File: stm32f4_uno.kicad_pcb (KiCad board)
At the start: 2 copper layers, 68.6 x 53.3 mm, 66 parts, among them J1 Barrel_Jack, J101 Digital/PWM, J102 Power, J103 Analog, J104 Digital/PWM, J105 Conn_ST_STDC14, J106 Ethernet, J107 STM32 GPIO, J108 STM32 GPIO, J109 STM32 GPIO, J110 STM32 GPIO, J111 STM32 GPIO, J2 SHOU HAN TYPE-C 16PIN 2MD(073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, U101 STM32F407VGT6, U201 AMS1117-5.0, U301 AMS1117-3.3, U501 SST26VF016BEUI-104I/SN, Y101 25MHz, Y102 32.768kHz

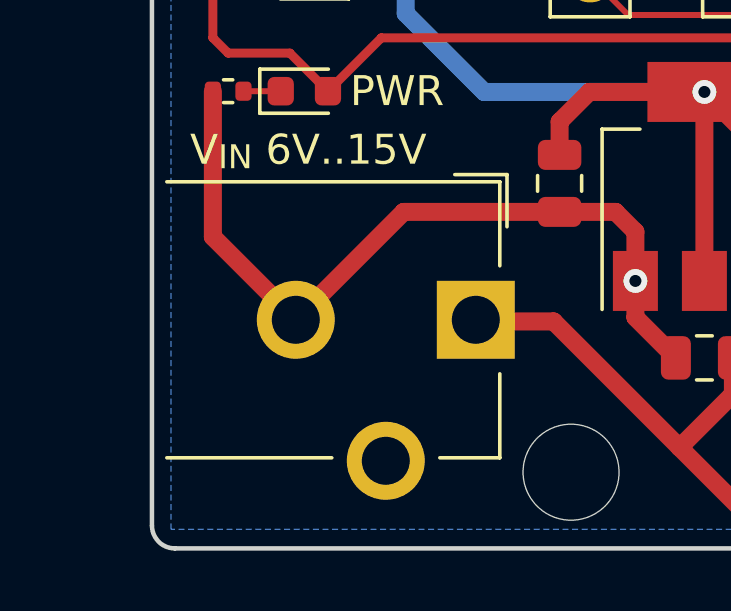
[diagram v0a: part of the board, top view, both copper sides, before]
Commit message: Add CUI Devices PJ-102AH 3D model and export PCB 3D model
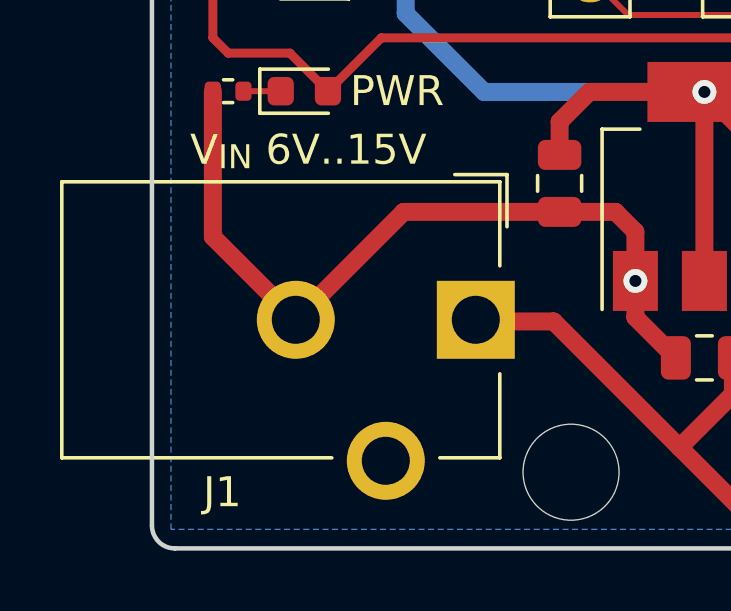
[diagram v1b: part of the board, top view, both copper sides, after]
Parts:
- J1: footprint Connector_BarrelJack:BarrelJack_CUI_PJ-102AH_Horizontal -> #Connector:CUI Devices PJ-102AH.pdf
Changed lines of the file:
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@@
     )
   )
-  (footprint "Connector_BarrelJack:BarrelJack_CUI_PJ-102AH_Horizontal" (layer "F.Cu")
+  (footprint "#Connector:CUI Devices PJ-102AH.pdf" (layer "F.Cu")
     (at 110.795 92.38 -90)
     (descr "Thin-pin DC Barrel Jack, https://cdn-shop.adafruit.com/datasheets/21mmdcjackDatasheet.pdf")
@@
     (property "Sheetfile" "stm32f4_uno.kicad_sch")
     (property "Sheetname" "")
-    (property "dnp" "")
     (property "exclude_from_bom" "")
     (property "isBasicPart" "NO")
@@
     (property "ki_keywords" "DC power barrel jack connector")
     (attr through_hole exclude_from_bom)
-    (fp_text reference "J1" (at 5.75 8.45) (layer "F.SilkS") hide
-        (effects (font (size 0.8 0.8) (thickness 0.15)))
-    )
-    (fp_text value "Barrel_Jack" (at -5.5 6.2) (layer "F.Fab") hide
-        (effects (font (size 0.8 0.8) (thickness 0.15)))
-    )
-    (fp_text user "${REFERENCE}" (at 0 6.5 90) (layer "F.Fab")
+    (fp_text reference "J1" (at 5.75 8.45) (layer "F.SilkS")
         (effects (font (size 1 1) (thickness 0.15)))
     )
+    (fp_text value "Barrel_Jack" (at -5.5 6.2) (layer "F.Fab")
+        (effects (font (size 1 1) (thickness 0.15)))
+    )
+    (fp_text user "${REFERENCE}" (at 0 6.5 -90) (layer "F.Fab")
+        (effects (font (size 1 1) (thickness 0.15)))
+    )
     (fp_line (start -4.84 -1.04) (end -3.1 -1.04)
       (stroke (width 0.12) (type solid)) (layer "F.SilkS"))
@@
     (fp_line (start -4.6 -0.8) (end -1.8 -0.8)
       (stroke (width 0.12) (type solid)) (layer "F.SilkS"))
-    (fp_line (start -4.6 10.3) (end -4.6 -0.8)
+    (fp_line (start -4.6 13.8) (end -4.6 -0.8)
       (stroke (width 0.12) (type solid)) (layer "F.SilkS"))
     (fp_line (start 1.8 -0.8) (end 4.6 -0.8)
@@
     (fp_line (start 4.6 -0.8) (end 4.6 1.2)
       (stroke (width 0.12) (type solid)) (layer "F.SilkS"))
-    (fp_line (start 4.6 4.8) (end 4.6 10.3)
+    (fp_line (start 4.6 4.8) (end 4.6 13.8)
+      (stroke (width 0.12) (type solid)) (layer "F.SilkS"))
+    (fp_line (start 4.6 13.8) (end -4.6 13.8)
       (stroke (width 0.12) (type solid)) (layer "F.SilkS"))
     (fp_line (start -5 -1.2) (end -1.8 -1.2)
@@
     (pad "3" thru_hole circle (at 4.7 3 270) (size 2.6 2.6) (drill 1.6) (layers "*.Cu" "*.Mask")
       (net 108 "unconnected-(J1-Pad3)") (pintype "passive+no_connect"))
-    (model "${KICAD6_3DMODEL_DIR}/Connector_BarrelJack.3dshapes/BarrelJack_CUI_PJ-102AH_Horizontal.wrl"
-      (offset (xyz 0 0 0))
-      (scale (xyz 1 1 1))
-      (rotate (xyz 0 0 0))
+    (model "${KIPRJMOD}/KiCad-Lib/#Connector.3dshapes/CUI Devices PJ-102AH.step"
+      (offset (xyz 0 -6.5 0))
+      (scale (xyz 1 1 1))
+      (rotate (xyz -90 0 90))
     )
   )
@@
     (pad "S1" thru_hole oval (at 4.32 1.075 270) (size 1 1.8) (drill oval 0.6 1.4) (layers "*.Cu" "*.Mask" "F.Paste")
       (net 1 "GND") (pinfunction "SHIELD") (pintype "passive"))
-    (model "${KIPRJMOD}/KiCad-Lib/#Connector.3dshapes/SHOU HAN TYPE-C 16PIN 2MD(073) (C2765186).wrl"
-      (offset (xyz 0 0 0))
-      (scale (xyz 1 1 1))
-      (rotate (xyz 0 0 0))
+    (model "${KIPRJMOD}/KiCad-Lib/#Connector.3dshapes/SHOU HAN TYPE-C 16PIN 2MD(073) (C2765186).step"
+      (offset (xyz -4.95 9.3 -1.6))
+      (scale (xyz 1 1 1))
+      (rotate (xyz 0 0 0))

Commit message: WIP
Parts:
- removed C201, C202: 22u 25V, Capacitor_SMD:C_0805_2012Metric
- removed U201: AMS1117-5.0, Package_TO_SOT_SMD:SOT-223-3_TabPin2
- added C603: 220u 50V, Capacitor_SMD:CP_Elec_10x10, F.Cu at (118.0, 89.5)
- added C604: 1u 50V, Capacitor_SMD:C_0805_2012Metric, F.Cu at (76.9, 69.0)
- added C605: 180u 35V, Capacitor_SMD:CP_Elec_10x12.6, F.Cu at (82.2, 88.3)
- added D601: SS34, Diode_SMD:D_SMA, F.Cu at (104.6, 70.3)
- added L601: 68uH 3A, Inductor_SMD:L_Chilisin_BMRG00101030, F.Cu at (106.3, 79.2)
- added U602: XL1509-5.0, Package_SO:SOIC-8_3.9x4.9mm_P1.27mm, F.Cu at (76.8, 74.4)
- moved D301 29.2 mm to (117.0, 58.1)
- moved R301 29.2 mm to (114.5, 58.1)
- moved D101 27.3 mm to (102.5, 53.8), turned to 0 degrees
- moved R102 27.3 mm to (105.1, 53.8), turned to 0 degrees
- moved D102 26.5 mm to (102.5, 52.0), turned to 0 degrees
- moved R103 26.5 mm to (105.1, 52.0), turned to 0 degrees
- moved D103 25.8 mm to (102.5, 50.2), turned to 0 degrees
- moved R104 25.8 mm to (105.1, 50.2), turned to 0 degrees
- moved D104 25.0 mm to (102.5, 48.4), turned to 0 degrees
- moved R105 25.0 mm to (105.1, 48.4), turned to 0 degrees
- moved D105 5.94 mm to (110.9, 66.0), turned to 90 degrees
- moved C112 2.29 mm to (130.2, 78.9)
- moved C302 1.63 mm to (125.4, 81.5)
- moved C301 1.55 mm to (125.4, 86.5)
- moved U301 1.51 mm to (130.2, 84.3)
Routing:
- net +3V3: track 248.7 -> 203.0 mm
- net /PC12/LED3_RED: track 28.8 -> 62.3 mm
- net /PC10/LED4_BLU: track 28.3 -> 58.5 mm
- net /PD3/LED1_GRN: track 31.7 -> 58.2 mm
- net GND: track 66.8 -> 41.1 mm
- net /PD1/LED2_ORG: track 30.3 -> 56.0 mm
- net +5V: track 78.4 -> 68.7 mm
- net /V_{IN}: track 45.4 -> 40.7 mm
- net /VBUS: track 14.9 -> 13.6 mm
- net Net-(D301-K): track 1.24 -> 0.00 mm
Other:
- board text added: "V_{IN} 6V..40V"
- board text removed: "V_{IN} 6V..15V"

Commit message: WIP
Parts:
- C503: renamed from C605; value 180u 35V -> 220uF 10V; footprint Capacitor_SMD:CP_Elec_10x12.6 -> Capacitor_Tantalum_SMD:CP_EIA-7343-31_Kemet-D
- renumbered C112 to C101, C106 to C102, C107 to C103, C108 to C104, C109 to C105, C110 to C106, C111 to C107, C116 to C108, C117 to C109, C113 to C110, C114 to C111, C115 to C112, C101 to C113, C103 to C114, C102 to C115, C119 to C116, C118 to C117, C104 to C118, C105 to C119, C501 to C301, C301 to C401, C302 to C402, C604 to C501, C603 to C502, D301 to D401, D601 to D501, J110 to J101, J101 to J102, J111 to J103, J107 to J104, J109 to J105, J102 to J106, J106 to J107, J104 to J109, J103 to J110, J105 to J111, J1 to J112, J2 to J201, JP102 to JP101, JP101 to JP102, L601 to L501, R106 to R101, R101 to R102, R102 to R103, R103 to R104, R104 to R105, R105 to R106, R401 to R201, R402 to R202, R403 to R203, R301 to R401, U501 to U301, U301 to U401, U602 to U501

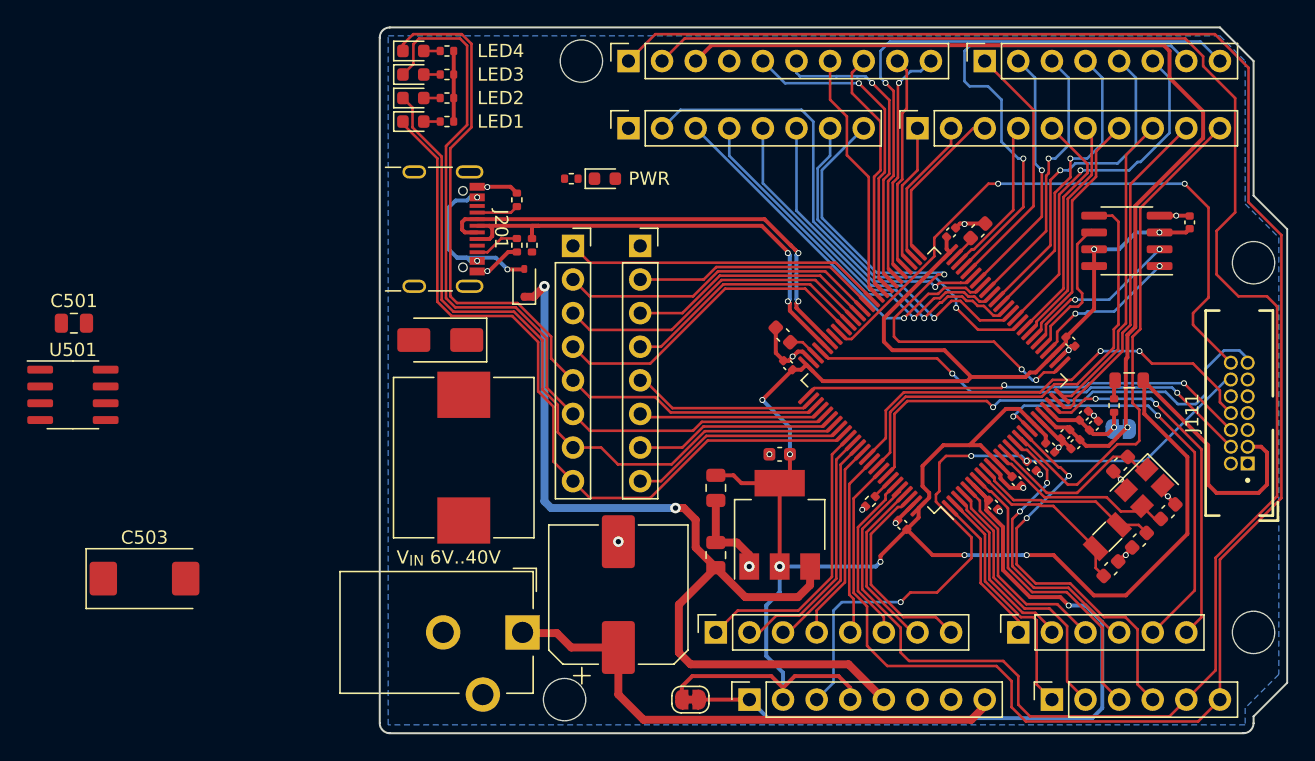
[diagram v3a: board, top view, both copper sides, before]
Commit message: Replaced 5V LDO for a 40V->5V buck converter
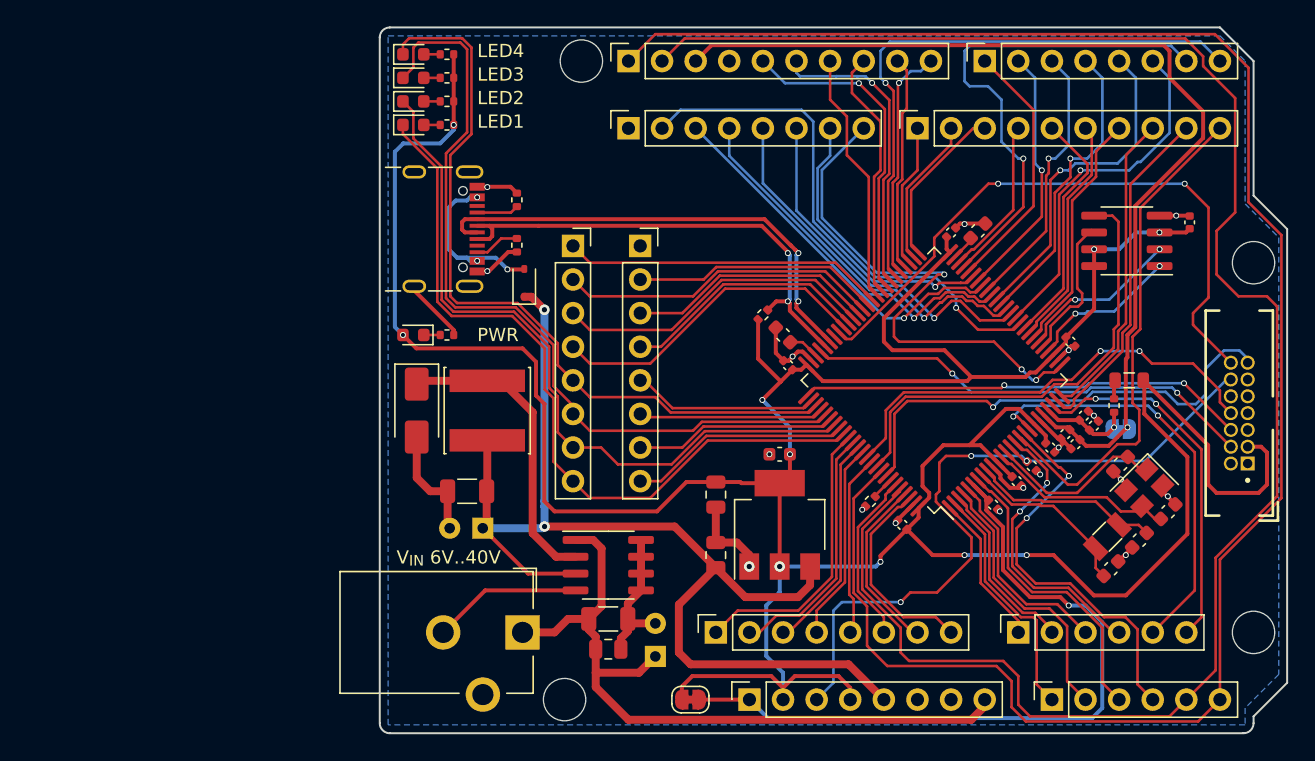
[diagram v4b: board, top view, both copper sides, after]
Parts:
- added C504: ?, Capacitor_THT:CP_Radial_D6.3mm_P2.50mm, B.Cu at (120.8, 94.2)
- added C505: ?, Capacitor_THT:CP_Radial_D6.3mm_P2.50mm, B.Cu at (107.8, 84.5)
- C502: value 220u 50V -> 10u 50V; footprint Capacitor_SMD:CP_Elec_10x10 -> Capacitor_SMD:C_1206_3216Metric
- C503: value 220uF 10V -> 47uF 10V; footprint Capacitor_Tantalum_SMD:CP_EIA-7343-31_Kemet-D -> Capacitor_SMD:C_1206_3216Metric
- L501: value 68uH 3A -> 68uH 1A; footprint Inductor_SMD:L_Chilisin_BMRG00101030 -> Inductor_SMD:L_Sunlord_SWPA6045S
- moved C501 47.3 mm to (117.3, 93.6)
- moved U501 42.5 mm to (117.3, 87.3)
- moved C503 25.3 mm to (106.6, 81.7), turned to 180 degrees
- moved D401 18.7 mm to (102.5, 69.9), turned to 180 degrees
- moved R203 18.2 mm to (129.0, 68.4), turned to 45 degrees
- moved R401 15.1 mm to (105.1, 69.9), turned to 180 degrees
- moved D501 5.62 mm to (102.8, 75.6), turned to -90 degrees
- moved L501 3.98 mm to (108.1, 75.6)
- moved C502 1.99 mm to (117.3, 91.4), turned to 0 degrees
- moved C402 0.51 mm to (125.4, 82.0)
- moved D101 0.25 mm to (102.5, 54.0)
- moved D102 0.25 mm to (102.5, 52.2)
- moved D103 0.25 mm to (102.5, 50.5)
- moved D104 0.25 mm to (102.5, 48.7)
- moved R103 0.25 mm to (105.1, 54.0)
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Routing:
- net +3V3: track 203.0 -> 263.7 mm, vias 8 -> 10
- net GND: track 41.1 -> 76.6 mm, vias 19 -> 18
- net /40V->5V/VOUT: track 0.00 -> 22.6 mm
- net +5V: track 68.7 -> 89.5 mm
- net /V_{IN}: track 40.7 -> 55.1 mm
- net Net-(D401-K): track 0.00 -> 1.24 mm
